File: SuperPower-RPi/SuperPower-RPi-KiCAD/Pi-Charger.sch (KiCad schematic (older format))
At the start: 0 parts

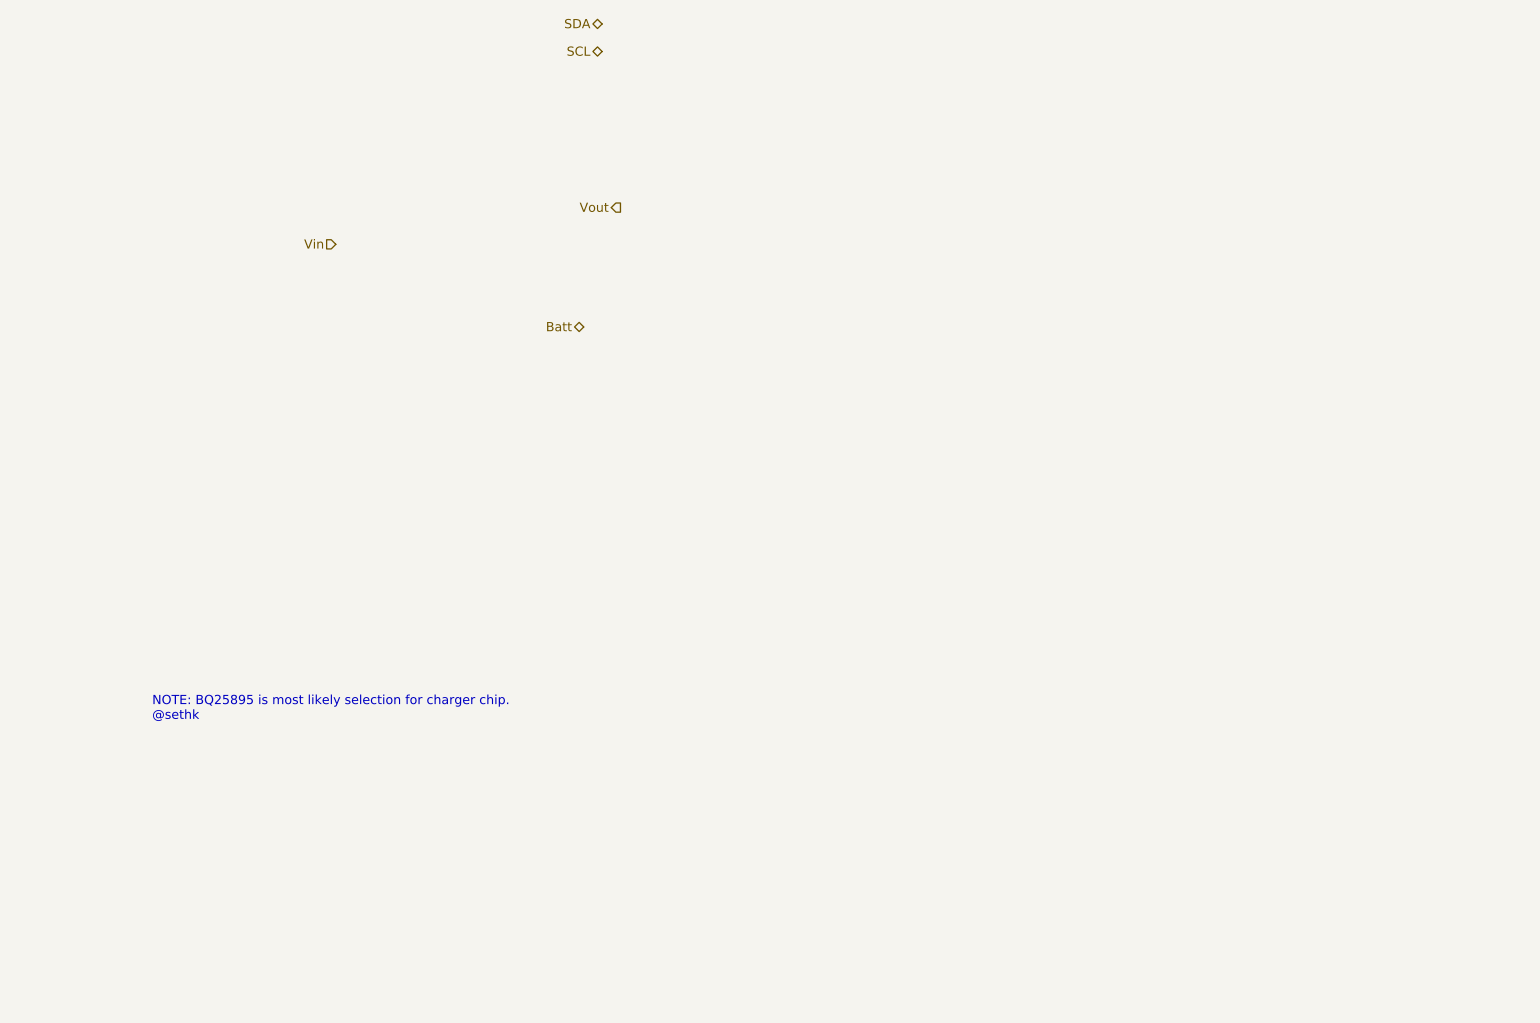
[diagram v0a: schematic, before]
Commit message: Added Charger chip to schem.  Need to put in passives.
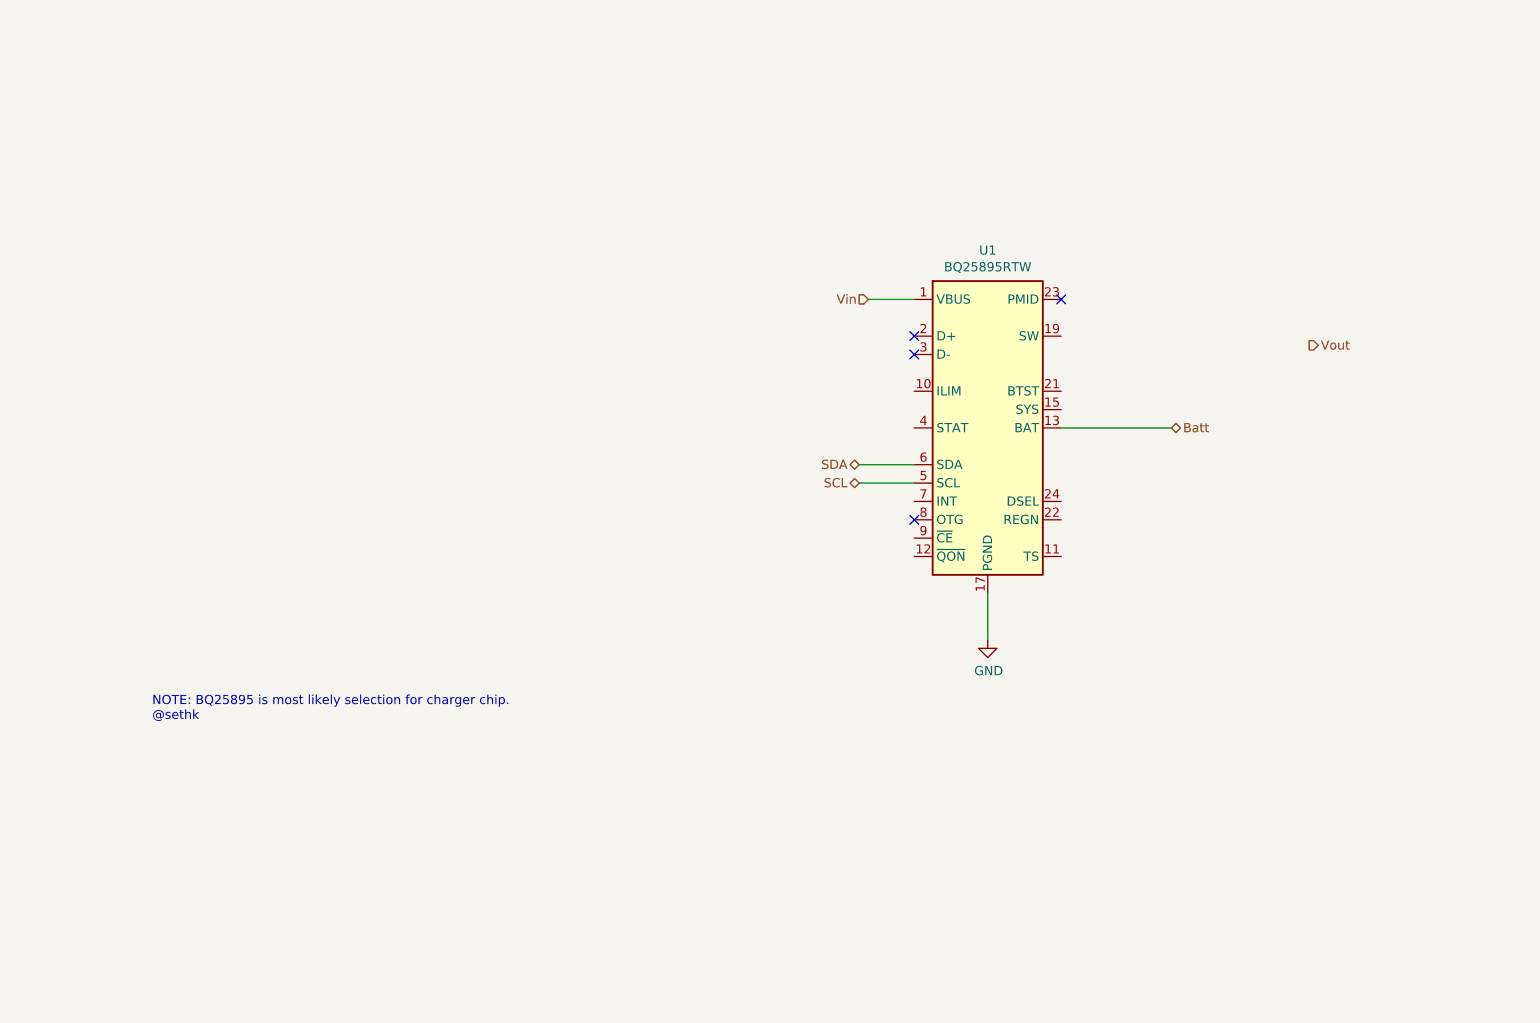
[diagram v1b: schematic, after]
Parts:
- added U1: BQ25895RTW, Package_DFN_QFN:Texas_S-PWQFN-N24_EP2.7x2.7mm_ThermalVias, symbol Battery_Management:BQ25895RTW
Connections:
- net Batt: now also U1.13 (BAT), U1.14 (BAT)
- net SCL: now also U1.5 (SCL)
- net SDA: now also U1.6 (SDA)
- net Vin: now also U1.1 (VBUS)
- new net: U1.15 (SYS), U1.16 (SYS)
- new net: U1.19 (SW), U1.20 (SW)
- new net GND: U1.17 (PGND), U1.18 (PGND), U1.25 (PGND)
- no-connect marks 0 -> 4
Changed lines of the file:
@@
 Comment4 ""
 $EndDescr
-Text HLabel 2950 2500 0    50   Input ~ 0
+Text HLabel 5850 2800 0    50   Input ~ 0
 Vin
-Text HLabel 4500 2300 0    50   Output ~ 0
+Text HLabel 8250 3050 2    50   Output ~ 0
 Vout
-Text HLabel 4300 2950 0    50   BiDi ~ 0
+Text HLabel 7500 3500 2    50   BiDi ~ 0
 Batt
-Text HLabel 4400 1300 0    50   BiDi ~ 0
+Text HLabel 5800 3700 0    50   BiDi ~ 0
 SDA
-Text HLabel 4400 1450 0    50   BiDi ~ 0
+Text HLabel 5800 3800 0    50   BiDi ~ 0
 SCL
 Text Notes 1950 5100 0    50   ~ 0
 NOTE: BQ25895 is most likely selection for charger chip.\n@sethk
+$Comp
+L Battery_Management:BQ25895RTW U1
+U 1 1 5F70253E
+P 6500 3500
+F 0 "U1" H 6500 4467 50  0000 C CNN
+F 1 "BQ25895RTW" H 6500 4376 50  0000 C CNN
+F 2 "Package_DFN_QFN:Texas_S-PWQFN-N24_EP2.7x2.7mm_ThermalVias" H 6400 4500 50  0001 C CNN
+F 3 "http://www.ti.com/lit/ds/symlink/bq25895.pdf" H 6300 4300 50  0001 C CNN
+	1    6500 3500
+	1    0    0    -1
+$EndComp
+Wire Wire Line
+	5800 3800 6100 3800
+Wire Wire Line
+	6100 3700 5800 3700
+Wire Wire Line
+	6900 3500 7500 3500
+$Comp
+L power:GND #PWR03
+U 1 1 5F70369C
+P 6500 4650
+F 0 "#PWR03" H 6500 4400 50  0001 C CNN
+F 1 "GND" H 6505 4477 50  0000 C CNN
+F 2 "" H 6500 4650 50  0001 C CNN
+F 3 "" H 6500 4650 50  0001 C CNN
+	1    6500 4650
+	1    0    0    -1
+$EndComp
+Wire Wire Line
+	6500 4400 6500 4650
+NoConn ~ 6100 3000
+NoConn ~ 6100 3100
+Wire Wire Line
+	5850 2800 6100 2800
+NoConn ~ 6900 2800
+NoConn ~ 6100 4000
 $EndSCHEMATC

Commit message: Added charger circuitry, and updated boost converter.
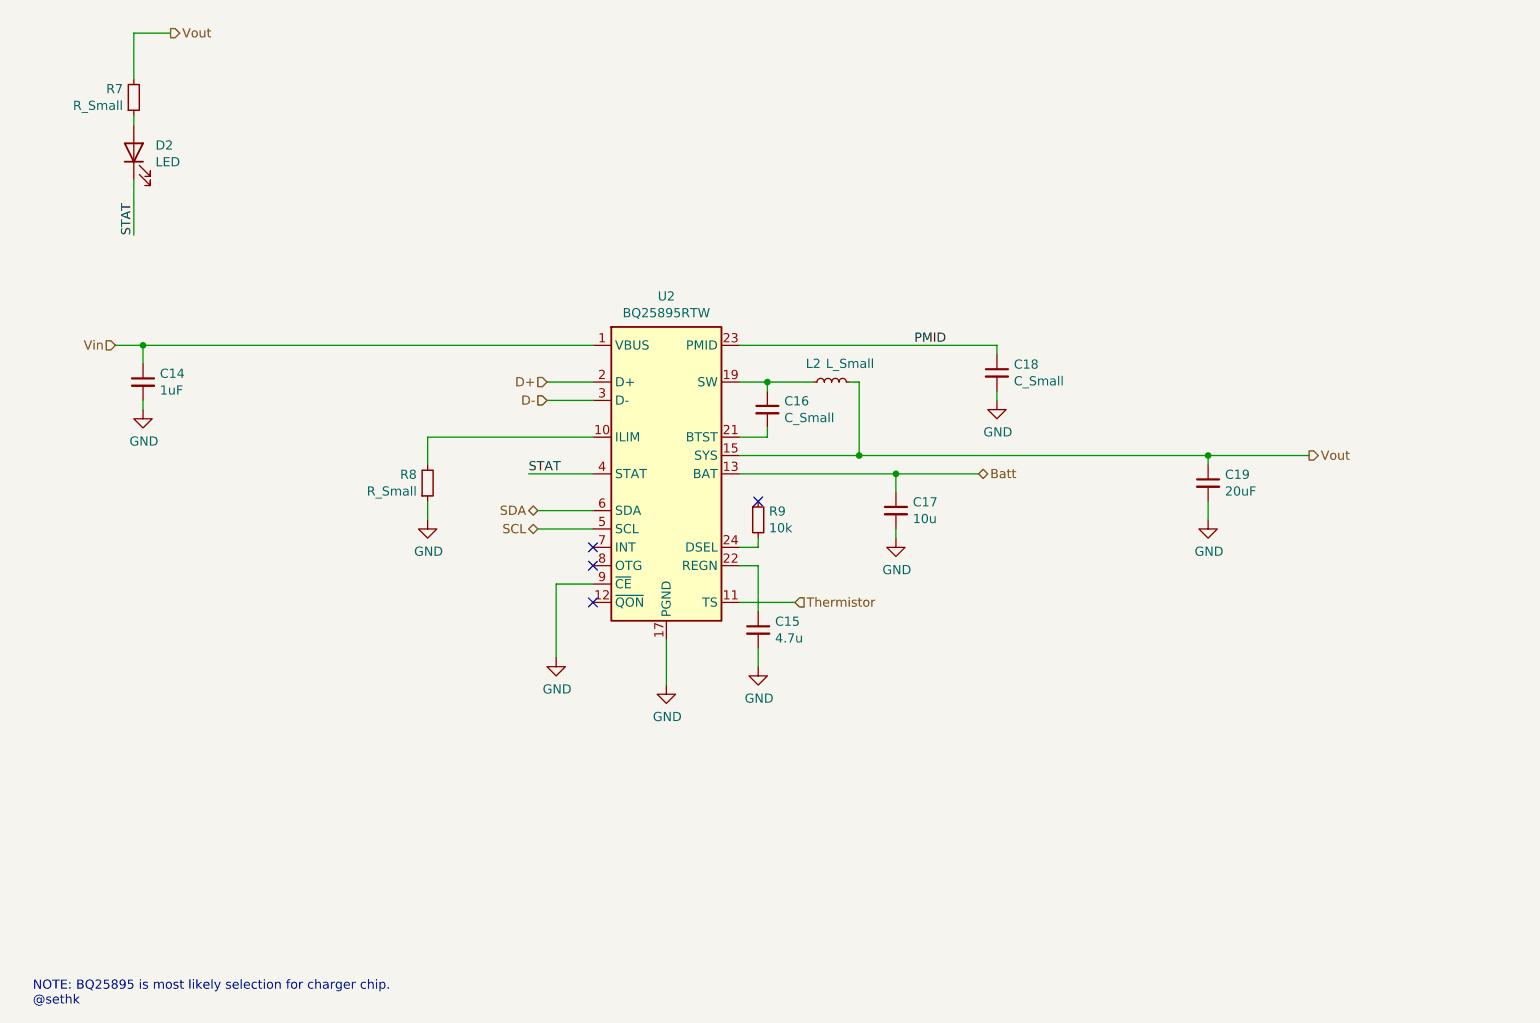
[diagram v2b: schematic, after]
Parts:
- removed U1: BQ25895RTW, Package_DFN_QFN:Texas_S-PWQFN-N24_EP2.7x2.7mm_ThermalVias, symbol Battery_Management:BQ25895RTW
- added C14: 1uF, symbol Device:C_Small
- added C15: 4.7u, symbol Device:C_Small
- added C16, C18: C_Small, symbol Device:C_Small
- added C17: 10u, symbol Device:C_Small
- added C19: 20uF, symbol Device:C_Small
- added D2: LED, symbol Device:LED
- added L2: L_Small, symbol Device:L_Small
- added R7, R8: R_Small, symbol Device:R_Small
- added R9: 10k, symbol Device:R_Small
- added U2: BQ25895RTW, Package_DFN_QFN:Texas_S-PWQFN-N24_EP2.7x2.7mm_ThermalVias, symbol Battery_Management:BQ25895RTW
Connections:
- net Batt: now also C17.1, U2.13 (BAT), U2.14 (BAT)
- net GND: now also C14.2, C15.2, C17.2, C18.2, C19.2, R8.1, U2.17 (PGND), U2.18 (PGND), U2.25 (PGND), U2.9 (~CE)
- net SCL: now also U2.5 (SCL)
- net SDA: now also U2.6 (SDA)
- net Vin: now also C14.1, U2.1 (VBUS)
- net Vout: now also C19.1, L2.2, R7.2, U2.15 (SYS), U2.16 (SYS)
- new net: R8.2, U2.10 (ILIM)
- new net: D2.2 (A), R7.1
- new net: C16.1, L2.1, U2.19 (SW), U2.20 (SW)
- new net: C15.1, U2.22 (REGN)
- new net: C16.2, U2.21 (BTST)
- new net: R9.2, U2.24 (DSEL)
- new net D+: U2.2 (D+)
- new net D-: U2.3 (D-)
- new net PMID: C18.1, U2.23 (PMID)
- new net STAT: D2.1 (K), U2.4 (STAT)
- new net Thermistor: U2.11 (TS)

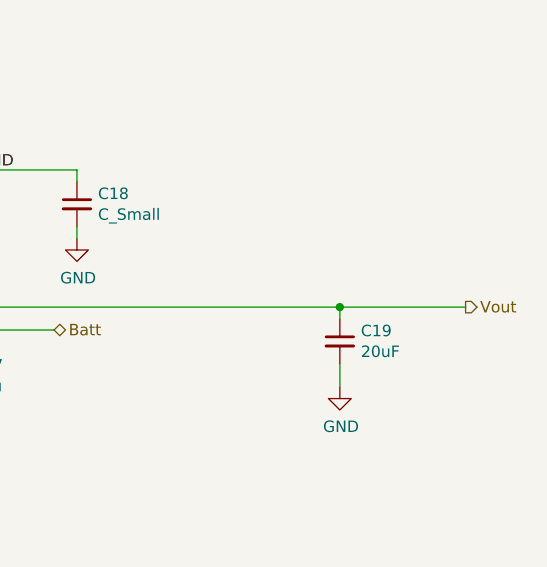
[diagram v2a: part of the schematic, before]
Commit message: Updated TPS61088 part to clear up ERC errors.
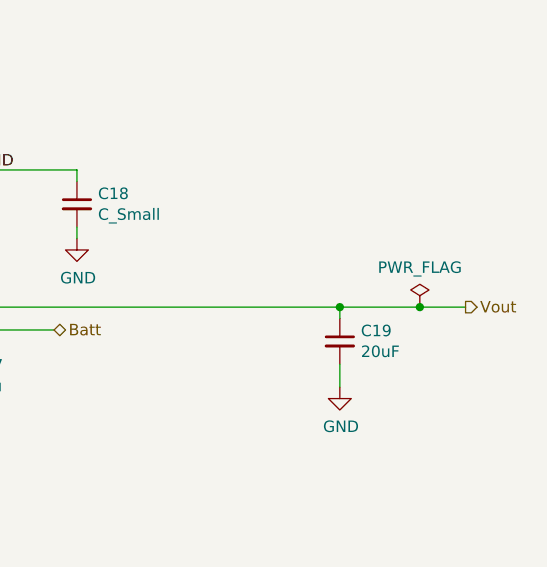
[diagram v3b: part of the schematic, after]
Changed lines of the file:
@@
 Connection ~ 7700 3650
 Wire Wire Line
-	7700 3650 8250 3650
+	7700 3650 8050 3650
 $Comp
 L power:GND #PWR0106
@@
 Text HLabel 4100 3350 0    50   Input ~ 0
 D-
+$Comp
+L power:PWR_FLAG #FLG0104
+U 1 1 5F7992CC
+P 8050 3650
+F 0 "#FLG0104" H 8050 3725 50  0001 C CNN
+F 1 "PWR_FLAG" H 8050 3823 50  0000 C CNN
+F 2 "" H 8050 3650 50  0001 C CNN
+F 3 "~" H 8050 3650 50  0001 C CNN
+	1    8050 3650
+	1    0    0    -1
+$EndComp
+Connection ~ 8050 3650
+Wire Wire Line
+	8050 3650 8250 3650
 $EndSCHEMATC

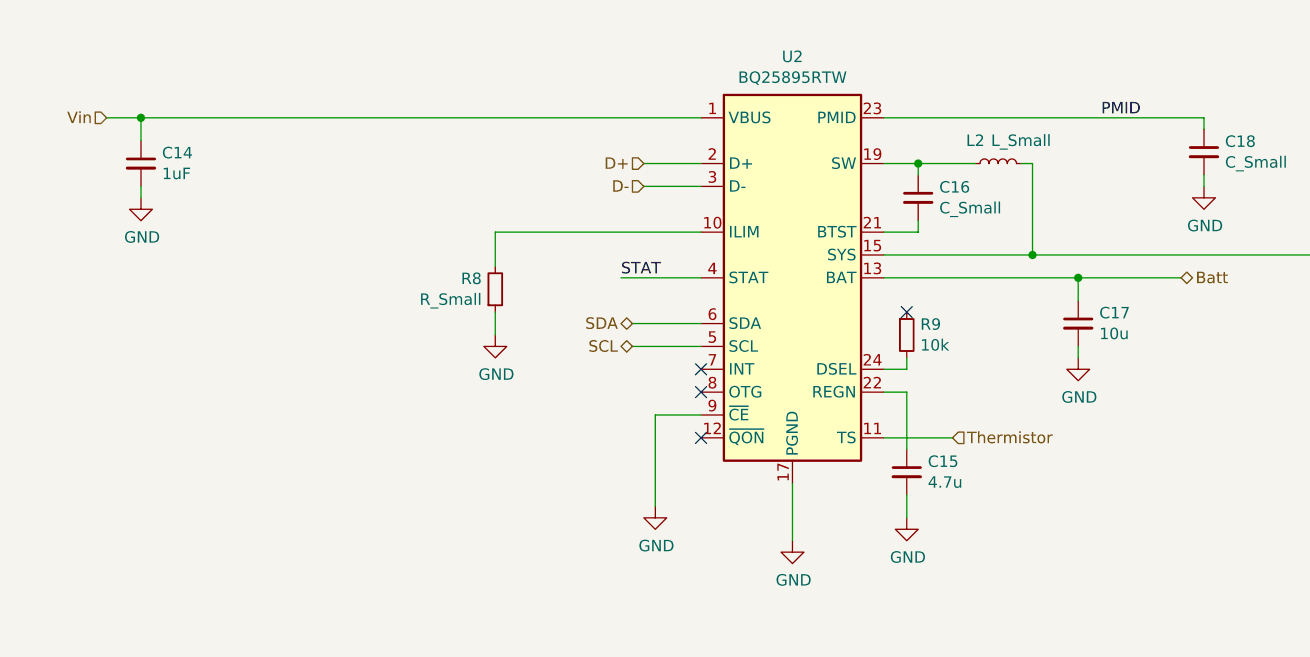
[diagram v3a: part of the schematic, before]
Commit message: Added overvoltag protection. Discussed on discord on 10/10/2020
(cherry picked from commit 123c8c775d478169a35a5854a68dc219ac457a44)
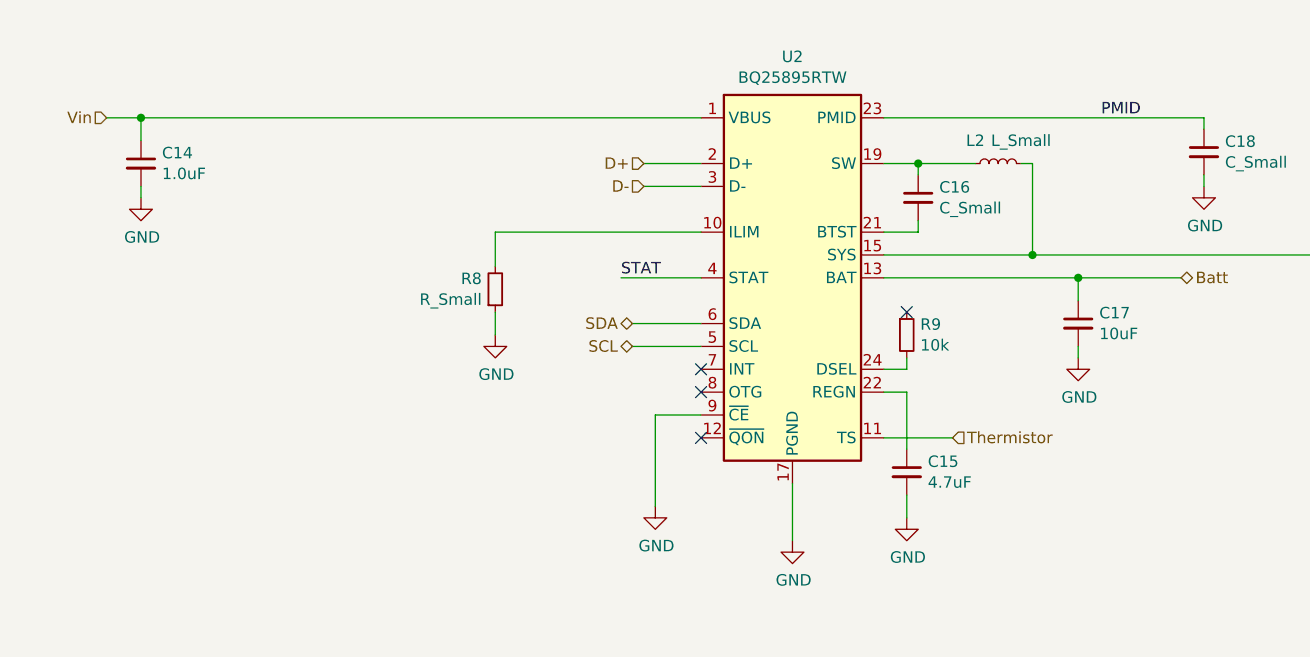
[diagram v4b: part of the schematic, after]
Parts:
- C14: value 1uF -> 1.0uF
- C15: value 4.7u -> 4.7uF
- C17: value 10u -> 10uF
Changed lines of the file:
@@
 P 1900 3250
 F 0 "C14" H 1992 3296 50  0000 L CNN
-F 1 "1uF" H 1992 3205 50  0000 L CNN
+F 1 "1.0uF" H 1992 3205 50  0000 L CNN
 F 2 "" H 1900 3250 50  0001 C CNN
 F 3 "~" H 1900 3250 50  0001 C CNN
@@
 P 5250 4600
 F 0 "C15" H 5342 4646 50  0000 L CNN
-F 1 "4.7u" H 5342 4555 50  0000 L CNN
+F 1 "4.7uF" H 5342 4555 50  0000 L CNN
 F 2 "" H 5250 4600 50  0001 C CNN
 F 3 "~" H 5250 4600 50  0001 C CNN
@@
 P 6000 3950
 F 0 "C17" H 6092 3996 50  0000 L CNN
-F 1 "10u" H 6092 3905 50  0000 L CNN
+F 1 "10uF" H 6092 3905 50  0000 L CNN
 F 2 "" H 6000 3950 50  0001 C CNN
 F 3 "~" H 6000 3950 50  0001 C CNN
